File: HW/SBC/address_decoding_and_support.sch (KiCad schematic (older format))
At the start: 7 parts, among them Q1 DS1813, SW1 RESET, U10 74LS138, U8 74HCT00, U9 74LS30, X1 4 MHz

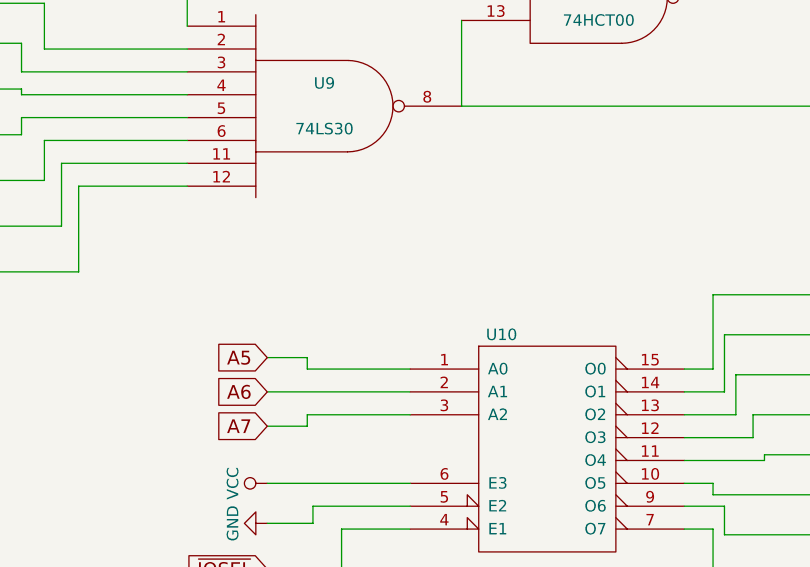
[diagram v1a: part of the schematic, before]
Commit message: Move dicoupling capacitators as close the chips as possible.
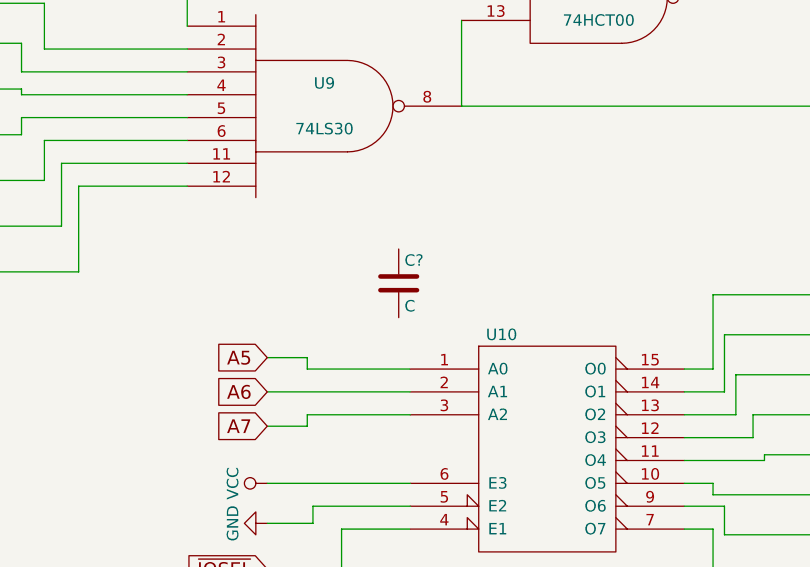
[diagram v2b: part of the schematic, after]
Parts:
- added C?: C, symbol C
- X1: footprint Oscillators:Oscillator_DIP-8 -> Housings_DIP:DIP-8_W7.62mm
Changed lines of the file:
@@
 F 0 "X1" H 1675 4900 50  0000 L CNN
 F 1 "4 MHz" H 1925 4400 50  0000 L CNN
-F 2 "Oscillators:Oscillator_DIP-8" H 2325 4300 50  0001 C CNN
+F 2 "Housings_DIP:DIP-8_W7.62mm" H 2325 4300 50  0001 C CNN
 F 3 "" H 1775 4650 50  0001 C CNN
 	1    1875 4650
@@
 $EndComp
 NoConn ~ 1675 1675
+$Comp
+L C C?
+U 1 1 59054EDF
+P 7275 3850
+F 0 "C?" H 7300 3950 50  0000 L CNN
+F 1 "C" H 7300 3750 50  0000 L CNN
+F 2 "" H 7313 3700 50  0001 C CNN
+F 3 "" H 7275 3850 50  0001 C CNN
+	1    7275 3850
+	1    0    0    -1
+$EndComp
 $EndSCHEMATC

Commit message: Schema changes to SBC
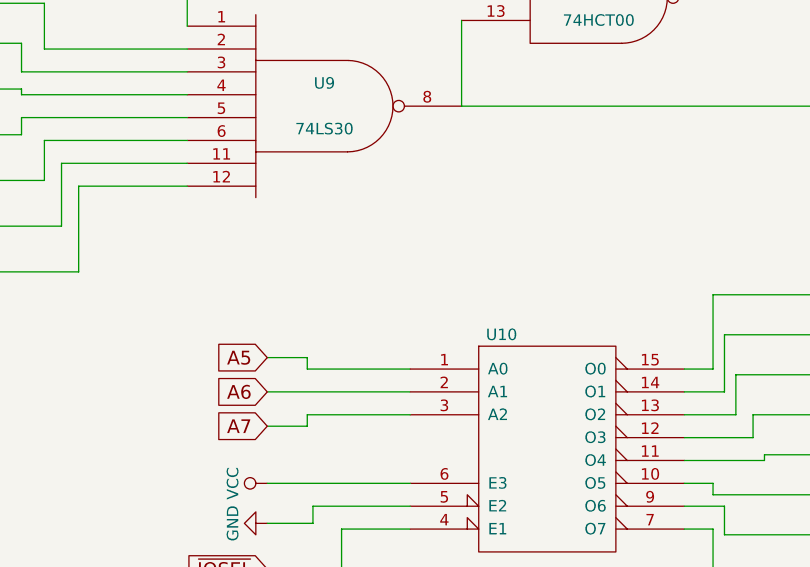
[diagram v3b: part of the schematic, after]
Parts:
- removed C?: C, symbol C
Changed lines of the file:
@@
 $EndComp
 NoConn ~ 1675 1675
-$Comp
-L C C?
-U 1 1 59054EDF
-P 7275 3850
-F 0 "C?" H 7300 3950 50  0000 L CNN
-F 1 "C" H 7300 3750 50  0000 L CNN
-F 2 "" H 7313 3700 50  0001 C CNN
-F 3 "" H 7275 3850 50  0001 C CNN
-	1    7275 3850
-	1    0    0    -1
-$EndComp
 $EndSCHEMATC

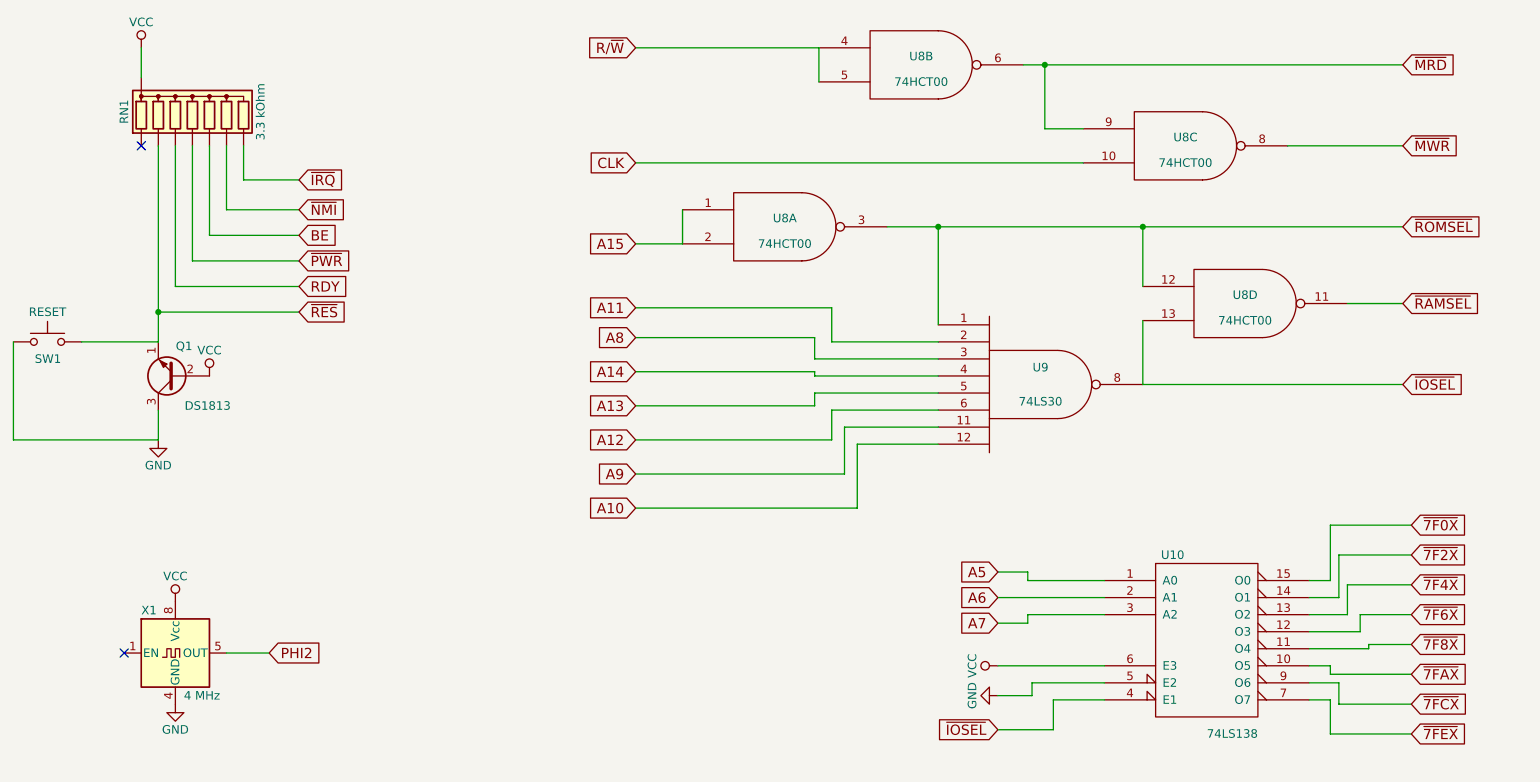
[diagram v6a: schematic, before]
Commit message: New schema. Adding a VIA and sound chip.
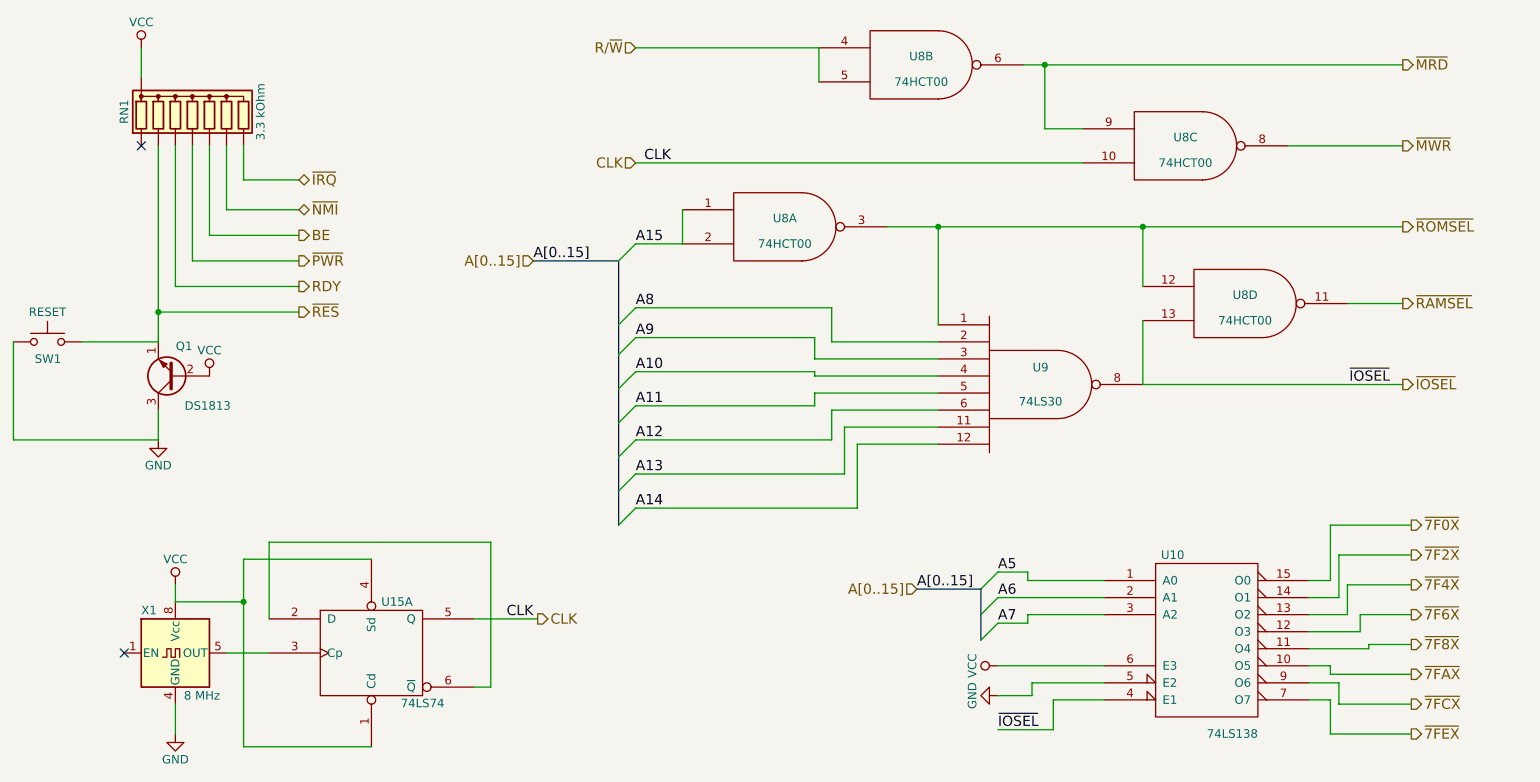
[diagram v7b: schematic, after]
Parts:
- added U15: 74LS74, symbol 74LS74
- X1: value 4 MHz -> 8 MHz
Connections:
- net A10: now also U9.4; no longer U9.12
- net A11: now also U9.5; no longer U9.2
- net A13: now also U9.11; no longer U9.5
- net A14: now also U9.12; no longer U9.4
- net A8: now also U9.2; no longer U9.3
- net A9: now also U9.3; no longer U9.11
- net CLK: now also U15.5 (Q)
- net GND: now also U15.7 (GND)
- net VCC: now also U15.1 (Cd), U15.14 (VCC), U15.4 (Sd)
- net PHI2: no longer names the net of X1.5 (OUT)
- net PHI2: now also U15.3 (Cp)
- new net: U15.2 (D), U15.6 (~Q)

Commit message: Moved IDE schematics (WIP) into pluto.
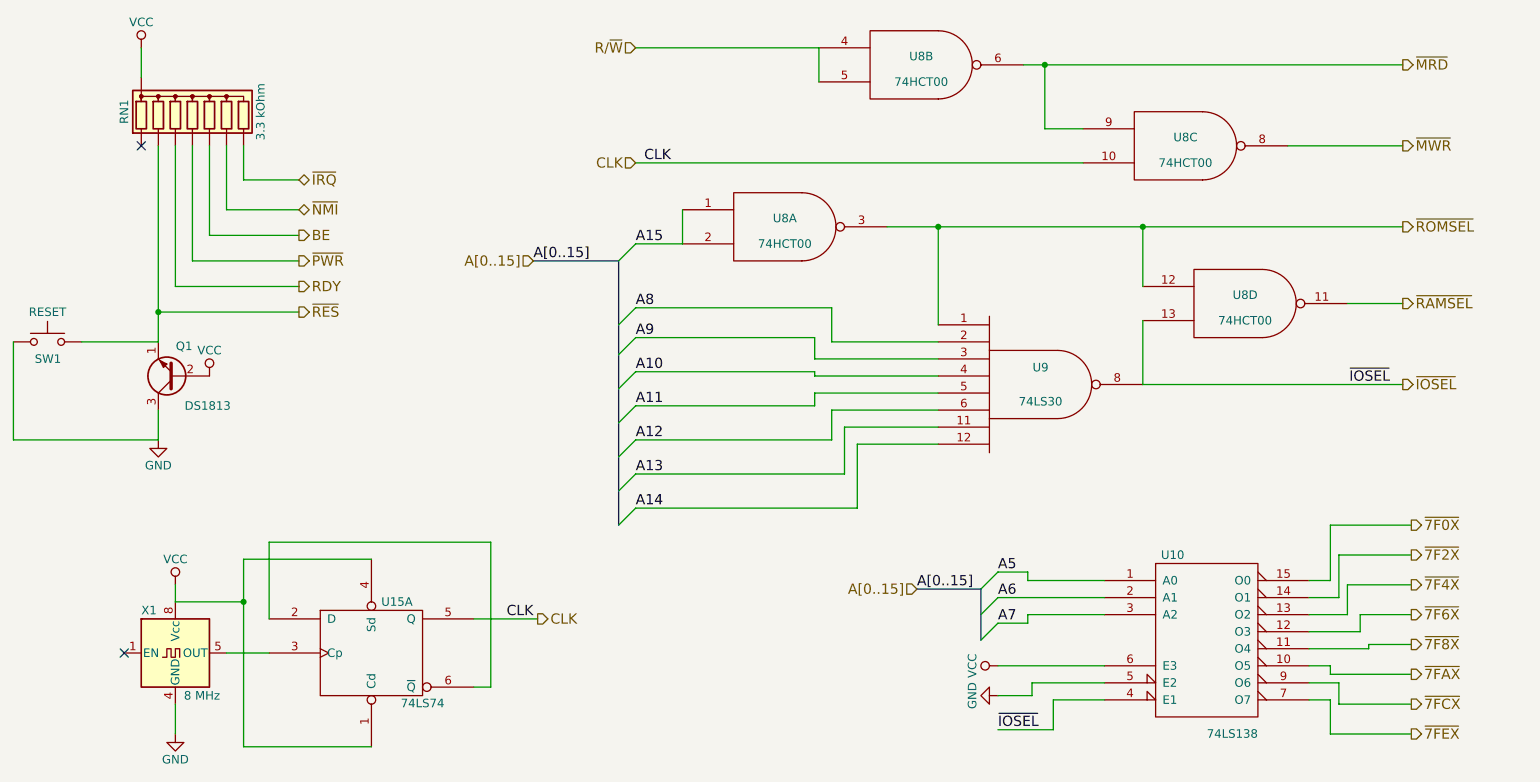
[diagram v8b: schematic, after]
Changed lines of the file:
@@
 EESchema Schematic File Version 2
+LIBS:pluto-rescue
 LIBS:power
 LIBS:device
@@
 $Descr A4 11693 8268
 encoding utf-8
-Sheet 5 7
+Sheet 5 8
 Title "Clock, pullups and decoding logic"
 Date "2017-03-25"
@@
 $EndComp
 Wire Wire Line
-	6050 2150 6350 2150
-Wire Wire Line
-	6350 2150 7550 2150
-Wire Wire Line
-	7550 2150 9075 2150
+	6050 2150 9075 2150
 Wire Wire Line
 	4850 2050 4850 2250
@@
 	5650 1300 5650 1100
 Wire Wire Line
-	6850 1200 6975 1200
-Wire Wire Line
-	6975 1200 9075 1200
+	6850 1200 9075 1200
 Wire Wire Line
 	6975 1200 6975 1575
@@
 	1675 1275 1675 1100
 Wire Wire Line
-	1775 1675 1775 2650
-Wire Wire Line
-	1775 2650 1775 2825
+	1775 1675 1775 2825
 Wire Wire Line
 	1775 2650 2600 2650
@@
 	2275 5200 3025 5200
 Wire Wire Line
-	2275 4100 2275 4350
-Wire Wire Line
-	2275 4350 2275 5200
+	2275 4100 2275 5200
 Wire Wire Line
 	2275 4350 1875 4350
@@
 	4475 3900 4575 3800
 Wire Bus Line
-	4475 3900 4475 3700
-Wire Bus Line
-	4475 3700 4475 3500
-Wire Bus Line
-	4475 3500 4475 3300
-Wire Bus Line
-	4475 3300 4475 3100
-Wire Bus Line
-	4475 3100 4475 2900
-Wire Bus Line
-	4475 2900 4475 2725
-Wire Bus Line
-	4475 2725 4475 2350
+	4475 2350 4475 3900
 Wire Bus Line
 	4475 2350 3975 2350
@@
 	6600 4575 6700 4475
 Wire Bus Line
-	6600 4575 6600 4425
-Wire Bus Line
-	6600 4425 6600 4275
+	6600 4275 6600 4575
 Wire Bus Line
 	6600 4275 6225 4275
